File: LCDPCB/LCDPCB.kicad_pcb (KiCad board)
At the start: 2 copper layers, 60 x 64 mm, 32 parts, among them J1 Sockets, J2 Hot Plug, J3 Programming Header, J4 Conn_01x08_Male, J5 Conn_01x08_Male, SW1 SW_Push, U1 STM32F091RCT6, U2 LD1117S12TR_SOT223

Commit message: fixed
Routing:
- net +3V0: track 16.6 -> 22.2 mm, vias 5 -> 7
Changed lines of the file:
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@@
   (via (at 124.714 72.136) (size 0.8) (drill 0.4) (layers "F.Cu" "B.Cu") (net 2))
   (segment (start 138.0422 90.4216) (end 138.0422 91.5602) (width 0.3) (layer "F.Cu") (net 3))
+  (segment (start 135.0542 80.9336) (end 135.0542 79.9362) (width 0.3) (layer "F.Cu") (net 3))
   (segment (start 131.7976 70.0278) (end 133.874 70.0278) (width 0.3) (layer "F.Cu") (net 3))
   (segment (start 136.652 77.724) (end 136.652 76.9338) (width 0.3) (layer "F.Cu") (net 3))
@@
   (segment (start 147.4124 80.9336) (end 148.2924 80.0536) (width 0.3) (layer "F.Cu") (net 3))
   (segment (start 138.5642 92.0822) (end 138.5642 92.8116) (width 0.3) (layer "F.Cu") (net 3))
+  (segment (start 136.906 79.0818) (end 137.0422 78.9456) (width 0.3) (layer "F.Cu") (net 3))
   (segment (start 144.5422 90.4216) (end 144.5422 91.1442) (width 0.3) (layer "F.Cu") (net 3))
   (segment (start 136.652 76.9338) (end 136.7282 76.8576) (width 0.3) (layer "F.Cu") (net 3))
+  (segment (start 135.0542 79.9362) (end 134.874 79.756) (width 0.3) (layer "F.Cu") (net 3))
+  (segment (start 136.906 80.772) (end 136.906 79.0818) (width 0.3) (layer "F.Cu") (net 3))
   (segment (start 135.0542 80.9336) (end 134.0167 80.9336) (width 0.3) (layer "F.Cu") (net 3))
   (segment (start 134.0167 80.9336) (end 132.6642 82.2861) (width 0.3) (layer "F.Cu") (net 3))
@@
   (via (at 145.854 92.456) (size 0.8) (drill 0.4) (layers "F.Cu" "B.Cu") (net 3))
   (via (at 132.6642 82.8476) (size 0.8) (drill 0.4) (layers "F.Cu" "B.Cu") (net 3))
+  (via (at 136.906 80.772) (size 0.8) (drill 0.4) (layers "F.Cu" "B.Cu") (net 3))
   (via (at 149.0472 80.0536) (size 0.8) (drill 0.4) (layers "F.Cu" "B.Cu") (net 3))
   (via (at 136.7282 76.8576) (size 0.8) (drill 0.4) (layers "F.Cu" "B.Cu") (net 3))
+  (via (at 134.874 79.756) (size 0.8) (drill 0.4) (layers "F.Cu" "B.Cu") (net 3))
+  (segment (start 134.874 79.756) (end 135.89 79.756) (width 0.3) (layer "B.Cu") (net 3))
+  (segment (start 135.89 79.756) (end 136.906 80.772) (width 0.3) (layer "B.Cu") (net 3))
   (segment (start 124.6928 66.28) (end 124.714 66.3012) (width 0.5) (layer "F.Cu") (net 4))
   (segment (start 145.2088 66.8274) (end 145.2342 66.802) (width 0.5) (layer "F.Cu") (net 4))
@@
     (connect_pads (clearance 0.3))
     (min_thickness 0.25) (filled_areas_thickness no)
-    (fill (thermal_gap 0.5) (thermal_bridge_width 0.5))
+    (fill yes (thermal_gap 0.5) (thermal_bridge_width 0.5))
     (polygon
       (pts
@@
   )
   (zone (net 70) (net_name "Net-(C4-Pad1)") (layer "F.Cu") (hatch edge 0.508)
+    (priority 1)
     (connect_pads (clearance 0.3))
     (min_thickness 0.25) (filled_areas_thickness no)
-    (fill (thermal_gap 0.5) (thermal_bridge_width 0.5))
+    (fill yes (thermal_gap 0.5) (thermal_bridge_width 0.5))
     (polygon
       (pts
@@
   )
   (zone (net 70) (net_name "Net-(C4-Pad1)") (layer "B.Cu") (hatch edge 0.508)
+    (priority 1)
     (connect_pads (clearance 0.3))
     (min_thickness 0.25) (filled_areas_thickness no)
-    (fill (thermal_gap 0.5) (thermal_bridge_width 0.5))
+    (fill yes (thermal_gap 0.5) (thermal_bridge_width 0.5))
     (polygon
       (pts
@@
     (connect_pads (clearance 0.3))
     (min_thickness 0.25) (filled_areas_thickness no)
-    (fill (thermal_gap 0.5) (thermal_bridge_width 0.5))
+    (fill yes (thermal_gap 0.5) (thermal_bridge_width 0.5))
     (polygon
       (pts

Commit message: do you love me now dad?
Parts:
- moved R2 7.90 mm to (139.8, 74.8)
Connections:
- net PB11 renamed RESET
- net PB14 renamed DC
- net PB3 renamed SCK
- net PB4 renamed MISO
- net PB5 renamed MOSI
- net PB8 renamed CS
- net PF11 renamed PD
- J4 pad 4: PA6 -> SCL
- J4 pad 5: PA7 -> SDA
- R5 pad 1: PA6 -> SCL
- R6 pad 1: PA7 -> SDA
- U1 pad 22: PA6 -> unconnected-(U1-Pad22)
- U1 pad 23: PA7 -> unconnected-(U1-Pad23)
- U1 pad 58: unconnected-(U1-Pad58) -> SCL
- U1 pad 59: unconnected-(U1-Pad59) -> SDA
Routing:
- net SCL: track 0.00 -> 61.1 mm, vias 0 -> 5
- net SDA: track 0.00 -> 59.6 mm, vias 0 -> 5
- net PA7: track 53.7 -> 0.00 mm, vias 5 -> 0
- net PA6: track 52.0 -> 0.00 mm, vias 5 -> 0
- net PD: track 50.2 -> 42.6 mm
- net PA13: track 78.3 -> 77.3 mm
- net MISO: track 60.4 -> 61.0 mm
- net GND: track 26.9 -> 27.4 mm
- net CS: track 54.2 -> 54.7 mm

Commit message: do you love me now dad?
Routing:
- net GND: track 27.4 -> 28.0 mm
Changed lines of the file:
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@@
   (segment (start 130.556 91.186) (end 127.762 93.98) (width 0.3) (layer "B.Cu") (net 1))
   (segment (start 154.19 70.878) (end 154.432 71.12) (width 0.3) (layer "B.Cu") (net 1))
+  (segment (start 122.174 59.944) (end 122.1232 59.9948) (width 0.5) (layer "F.Cu") (net 2))
   (segment (start 137.5422 78.9456) (end 137.5422 77.9081) (width 0.3) (layer "F.Cu") (net 2))
   (segment (start 157.5 81.006) (end 157.48 81.026) (width 0.25) (layer "F.Cu") (net 2))
   (segment (start 140.737 75.205) (end 141.732 76.2) (width 0.25) (layer "F.Cu") (net 2))
   (segment (start 134.3406 72.6186) (end 134.366 72.644) (width 0.3) (layer "F.Cu") (net 2))
-  (segment (start 122.1232 59.9948) (end 122.174 59.944) (width 0.5) (layer "F.Cu") (net 2))
   (segment (start 127.254 71.0056) (end 127.254 72.136) (width 0.3) (layer "F.Cu") (net 2))
   (segment (start 140.737 74.763) (end 140.737 75.205) (width 0.25) (layer "F.Cu") (net 2))
@@
   (segment (start 138.43 77.0203) (end 138.43 76.5738) (width 0.3) (layer "F.Cu") (net 2))
   (segment (start 134.0167 86.4336) (end 132.6642 85.0811) (width 0.3) (layer "F.Cu") (net 2))
-  (segment (start 122.1232 61.0532) (end 122.1232 59.9948) (width 0.5) (layer "F.Cu") (net 2))
   (segment (start 144.0422 92.2842) (end 144.214 92.456) (width 0.3) (layer "F.Cu") (net 2))
   (segment (start 161.5152 84.3568) (end 161.544 84.328) (width 0.3) (layer "F.Cu") (net 2))
@@
   (segment (start 141.478 76.2) (end 141.732 76.2) (width 0.3) (layer "F.Cu") (net 2))
   (segment (start 146.5302 81.4336) (end 147.4736 81.4336) (width 0.3) (layer "F.Cu") (net 2))
+  (segment (start 122.1232 59.9948) (end 122.1232 61.6432) (width 0.5) (layer "F.Cu") (net 2))
   (segment (start 147.4736 81.4336) (end 147.828 81.788) (width 0.3) (layer "F.Cu") (net 2))
   (segment (start 157.5 79.67) (end 157.5 81.006) (width 0.25) (layer "F.Cu") (net 2))

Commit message: renamed
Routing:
- net GND: track 28.0 -> 27.4 mm
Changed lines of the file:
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@@
   (segment (start 130.556 91.186) (end 127.762 93.98) (width 0.3) (layer "B.Cu") (net 1))
   (segment (start 154.19 70.878) (end 154.432 71.12) (width 0.3) (layer "B.Cu") (net 1))
-  (segment (start 122.174 59.944) (end 122.1232 59.9948) (width 0.5) (layer "F.Cu") (net 2))
   (segment (start 137.5422 78.9456) (end 137.5422 77.9081) (width 0.3) (layer "F.Cu") (net 2))
   (segment (start 157.5 81.006) (end 157.48 81.026) (width 0.25) (layer "F.Cu") (net 2))
   (segment (start 140.737 75.205) (end 141.732 76.2) (width 0.25) (layer "F.Cu") (net 2))
   (segment (start 134.3406 72.6186) (end 134.366 72.644) (width 0.3) (layer "F.Cu") (net 2))
+  (segment (start 122.1232 59.9948) (end 122.174 59.944) (width 0.5) (layer "F.Cu") (net 2))
   (segment (start 127.254 71.0056) (end 127.254 72.136) (width 0.3) (layer "F.Cu") (net 2))
   (segment (start 140.737 74.763) (end 140.737 75.205) (width 0.25) (layer "F.Cu") (net 2))
@@
   (segment (start 138.43 77.0203) (end 138.43 76.5738) (width 0.3) (layer "F.Cu") (net 2))
   (segment (start 134.0167 86.4336) (end 132.6642 85.0811) (width 0.3) (layer "F.Cu") (net 2))
+  (segment (start 122.1232 61.0532) (end 122.1232 59.9948) (width 0.5) (layer "F.Cu") (net 2))
   (segment (start 144.0422 92.2842) (end 144.214 92.456) (width 0.3) (layer "F.Cu") (net 2))
   (segment (start 161.5152 84.3568) (end 161.544 84.328) (width 0.3) (layer "F.Cu") (net 2))
@@
   (segment (start 141.478 76.2) (end 141.732 76.2) (width 0.3) (layer "F.Cu") (net 2))
   (segment (start 146.5302 81.4336) (end 147.4736 81.4336) (width 0.3) (layer "F.Cu") (net 2))
-  (segment (start 122.1232 59.9948) (end 122.1232 61.6432) (width 0.5) (layer "F.Cu") (net 2))
   (segment (start 147.4736 81.4336) (end 147.828 81.788) (width 0.3) (layer "F.Cu") (net 2))
   (segment (start 157.5 79.67) (end 157.5 81.006) (width 0.25) (layer "F.Cu") (net 2))

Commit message: edits
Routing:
- net +3V0: track 22.2 -> 25.2 mm, vias 7 -> 9
- net SCL: track 61.1 -> 59.8 mm
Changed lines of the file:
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@@
   (via (at 132.6642 84.4876) (size 0.8) (drill 0.4) (layers "F.Cu" "B.Cu") (net 2))
   (via (at 124.714 72.136) (size 0.8) (drill 0.4) (layers "F.Cu" "B.Cu") (net 2))
+  (segment (start 135.0542 80.0838) (end 135.0542 79.8298) (width 0.3) (layer "F.Cu") (net 3))
   (segment (start 138.0422 90.4216) (end 138.0422 91.5602) (width 0.3) (layer "F.Cu") (net 3))
-  (segment (start 135.0542 80.9336) (end 135.0542 79.9362) (width 0.3) (layer "F.Cu") (net 3))
+  (segment (start 134.3406 69.5612) (end 135.8552 69.5612) (width 0.3) (layer "F.Cu") (net 3))
   (segment (start 131.7976 70.0278) (end 133.874 70.0278) (width 0.3) (layer "F.Cu") (net 3))
   (segment (start 136.652 77.724) (end 136.652 76.9338) (width 0.3) (layer "F.Cu") (net 3))
@@
   (segment (start 144.5422 90.4216) (end 144.5422 91.1442) (width 0.3) (layer "F.Cu") (net 3))
   (segment (start 136.652 76.9338) (end 136.7282 76.8576) (width 0.3) (layer "F.Cu") (net 3))
-  (segment (start 135.0542 79.9362) (end 134.874 79.756) (width 0.3) (layer "F.Cu") (net 3))
+  (segment (start 135.0542 80.9336) (end 135.0542 80.0838) (width 0.3) (layer "F.Cu") (net 3))
   (segment (start 136.906 80.772) (end 136.906 79.0818) (width 0.3) (layer "F.Cu") (net 3))
+  (segment (start 135.8552 69.5612) (end 135.89 69.596) (width 0.3) (layer "F.Cu") (net 3))
   (segment (start 135.0542 80.9336) (end 134.0167 80.9336) (width 0.3) (layer "F.Cu") (net 3))
+  (segment (start 120.012 77.47) (end 120.65 77.47) (width 0.25) (layer "F.Cu") (net 3))
+  (segment (start 120.65 77.47) (end 121.412 76.708) (width 0.25) (layer "F.Cu") (net 3))
   (segment (start 134.0167 80.9336) (end 132.6642 82.2861) (width 0.3) (layer "F.Cu") (net 3))
+  (segment (start 135.0542 79.8298) (end 135.128 79.756) (width 0.3) (layer "F.Cu") (net 3))
   (segment (start 146.5302 80.9336) (end 147.4124 80.9336) (width 0.3) (layer "F.Cu") (net 3))
   (segment (start 132.6642 82.2861) (end 132.6642 82.8476) (width 0.3) (layer "F.Cu") (net 3))
@@
   (via (at 132.6642 82.8476) (size 0.8) (drill 0.4) (layers "F.Cu" "B.Cu") (net 3))
   (via (at 136.906 80.772) (size 0.8) (drill 0.4) (layers "F.Cu" "B.Cu") (net 3))
+  (via (at 135.89 69.596) (size 0.8) (drill 0.4) (layers "F.Cu" "B.Cu") (net 3))
   (via (at 149.0472 80.0536) (size 0.8) (drill 0.4) (layers "F.Cu" "B.Cu") (net 3))
   (via (at 136.7282 76.8576) (size 0.8) (drill 0.4) (layers "F.Cu" "B.Cu") (net 3))
-  (via (at 134.874 79.756) (size 0.8) (drill 0.4) (layers "F.Cu" "B.Cu") (net 3))
-  (segment (start 134.874 79.756) (end 135.89 79.756) (width 0.3) (layer "B.Cu") (net 3))
+  (via (at 135.128 79.756) (size 0.8) (drill 0.4) (layers "F.Cu" "B.Cu") (net 3))
+  (via (at 121.412 76.708) (size 0.8) (drill 0.4) (layers "F.Cu" "B.Cu") (net 3))
+  (segment (start 135.128 79.756) (end 135.89 79.756) (width 0.3) (layer "B.Cu") (net 3))
   (segment (start 135.89 79.756) (end 136.906 80.772) (width 0.3) (layer "B.Cu") (net 3))
   (segment (start 124.6928 66.28) (end 124.714 66.3012) (width 0.5) (layer "F.Cu") (net 4))
@@
   (segment (start 139.942 87.364) (end 139.942 87.11) (width 0.3) (layer "F.Cu") (net 22))
   (segment (start 119.1362 80.0354) (end 119.1362 80.0202) (width 0.3) (layer "F.Cu") (net 22))
-  (segment (start 115.515106 99.06) (end 114.3 99.06) (width 0.3) (layer "F.Cu") (net 22))
   (segment (start 119.1362 80.0202) (end 119.126 80.01) (width 0.3) (layer "F.Cu") (net 22))
   (segment (start 124.714 97.282) (end 124.46 97.536) (width 0.3) (layer "F.Cu") (net 22))

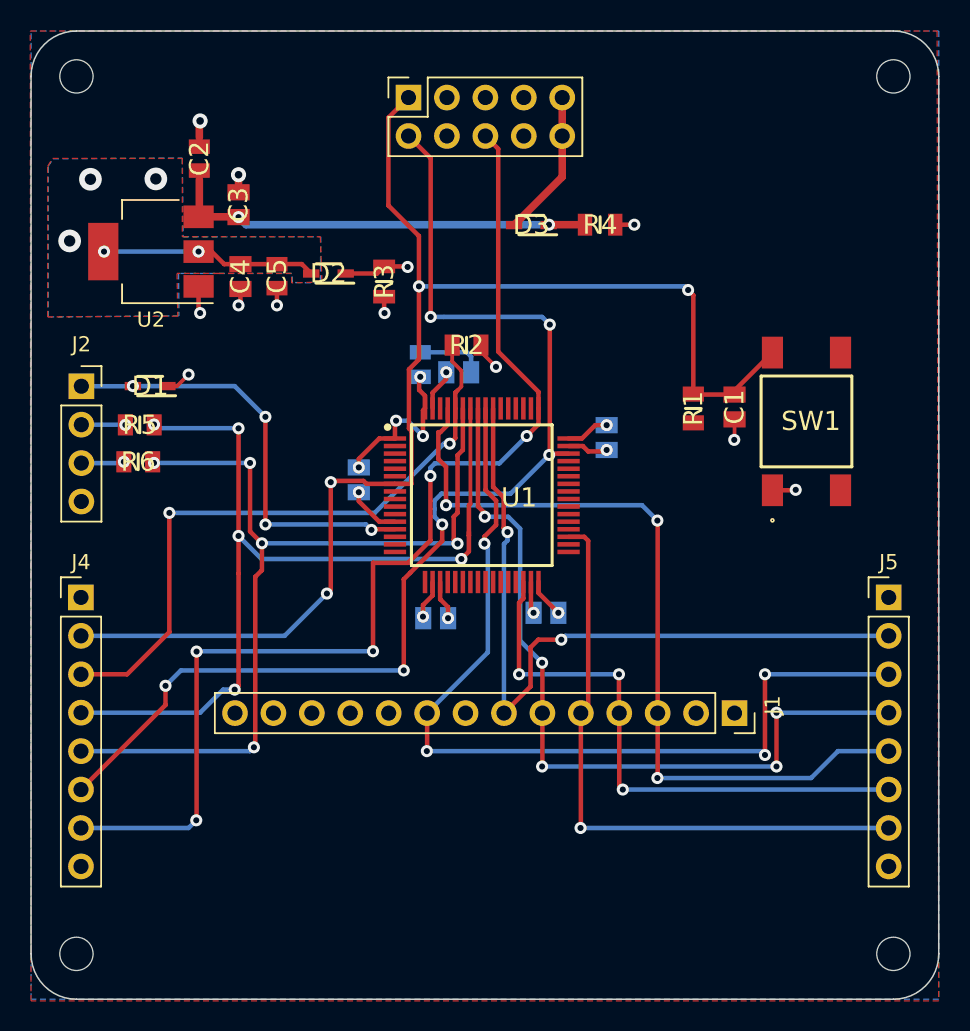
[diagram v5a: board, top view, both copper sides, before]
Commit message: remove via from pad v2
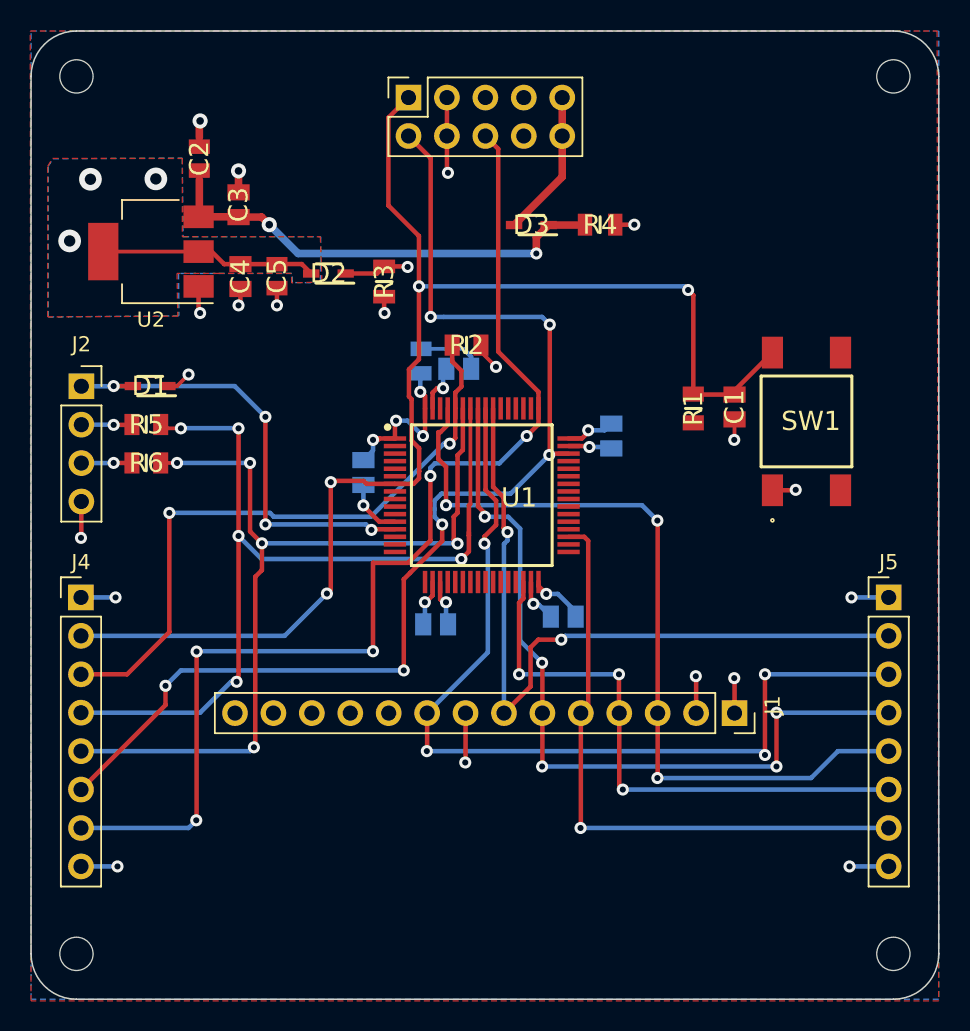
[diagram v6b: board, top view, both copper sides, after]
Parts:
- moved C9 1.17 mm to (146.2, 92.7)
- moved C7 0.57 mm to (133.0, 83.2)
- moved R6 0.54 mm to (118.6, 82.5)
- moved R5 0.43 mm to (118.6, 80.0)
- moved C8 0.41 mm to (137.7, 93.2)
- moved C10 0.32 mm to (149.4, 80.8)
- moved FB1 0.23 mm to (136.8, 75.8)
- moved C6 0.23 mm to (139.3, 76.3)
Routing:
- net GND: track 27.4 -> 45.0 mm, vias 15 -> 20
- net +3V0: track 25.2 -> 37.4 mm, vias 9 -> 13
- net +5V: track 28.3 -> 30.5 mm
- net +3.3V: track 28.9 -> 30.1 mm
- net SCL: track 59.8 -> 59.2 mm
- net SDA: track 59.6 -> 59.0 mm
- net NRST: track 89.1 -> 89.6 mm
- net Net-(J2-Pad3): track 2.85 -> 3.35 mm
- net Net-(C4-Pad1): vias 2 -> 0

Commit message: free of errors
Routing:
- net GND: track 45.0 -> 32.5 mm, vias 20 -> 16
- net Net-(C4-Pad1): track 14.3 -> 25.8 mm, vias 0 -> 3
- net +3V0: track 37.4 -> 26.1 mm, vias 13 -> 10
- net NRST: track 89.6 -> 88.6 mm, vias 4 -> 3
- net (no net): vias 3 -> 0
